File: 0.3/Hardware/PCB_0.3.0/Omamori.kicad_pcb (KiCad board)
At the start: 2 copper layers, 25 x 35 mm, 28 parts, among them J1 Conn_01x04_Female, U1 BQ25570, U3 ATtiny85, U4 TS-1233

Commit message: Unfinished update. Serial communication still unfinished.
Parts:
- removed the U3 at (18.0, 19.5)
- added REF**: Pin_D1.0mm_L10.0mm, Connector_Pin:Pin_D1.0mm_L10.0mm, F.Cu at (25.0, 15.0)
- added U2: ATtiny85-20S, Package_SO:SOIC-8W_5.3x5.3mm_P1.27mm, B.Cu at (18.0, 21.0)
- C_ref1: value 0.01uF -> 10nF
- C_super1: value 640mF -> 1F; footprint own_footprints:Supercap -> own_footprints:Supercap_1F
- moved U3 13.3 mm to (18.0, 15.0), turned to 0 degrees
- moved R_set1 2.38 mm to (32.1, 28.9), turned to 0 degrees
- moved R_set2 2.19 mm to (33.9, 30.4)
- moved R_LED3 1.34 mm to (21.1, 24.7)
- moved R_LED1 0.60 mm to (19.9, 27.7)
- moved R_LED2 0.60 mm to (19.9, 26.2)
- moved C_super1 0.50 mm to (25.0, 37.2)
- renumbered D3 to D1, D1 to D2, D2 to D3, U4 to U3
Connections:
- U3 pad 1: (no net) -> /Reset
- U3 pad 2: /Reset -> GND
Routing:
- net GND: track 183.4 -> 209.4 mm, vias 5 -> 4
- net /Vcc_ATTiny: track 56.5 -> 44.5 mm, vias 0 -> 2
- net /VCC_LED1: track 17.3 -> 9.56 mm
- net Net-(R_set1-Pad2): track 13.0 -> 20.0 mm
- net /Tx: track 30.3 -> 33.3 mm
- net /Reset: track 11.5 -> 14.3 mm
- net /Rx: track 31.9 -> 29.2 mm, vias 2 -> 0
- net Net-(Sol_1-Pad2): track 32.3 -> 34.9 mm
- net /VCC_LED3: track 6.72 -> 9.11 mm
- net /Vr_div: track 4.81 -> 7.13 mm
- net /Vbat: track 29.5 -> 28.7 mm
- net /VCC_LED2: track 10.3 -> 11.0 mm
- net Net-(R_LED1-Pad1): track 7.70 -> 8.30 mm
- net (no net): vias 1 -> 0
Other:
- net class Default removed

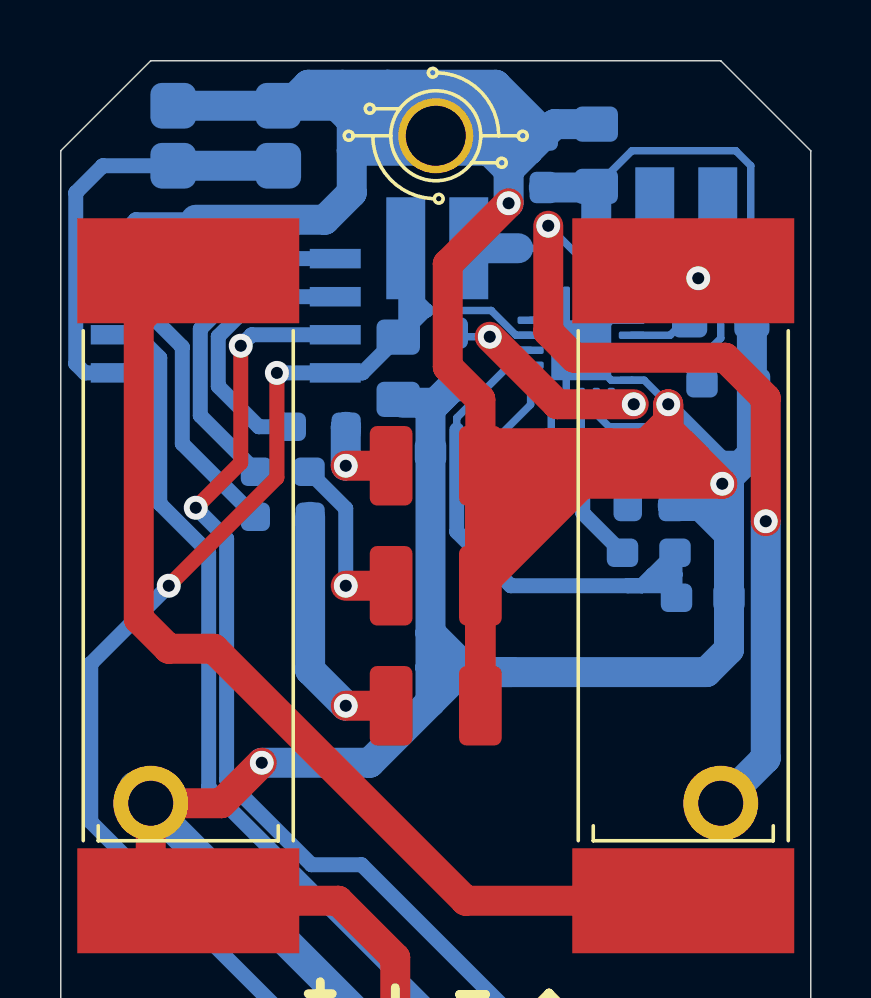
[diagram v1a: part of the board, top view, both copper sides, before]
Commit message: Voltage measurement update.
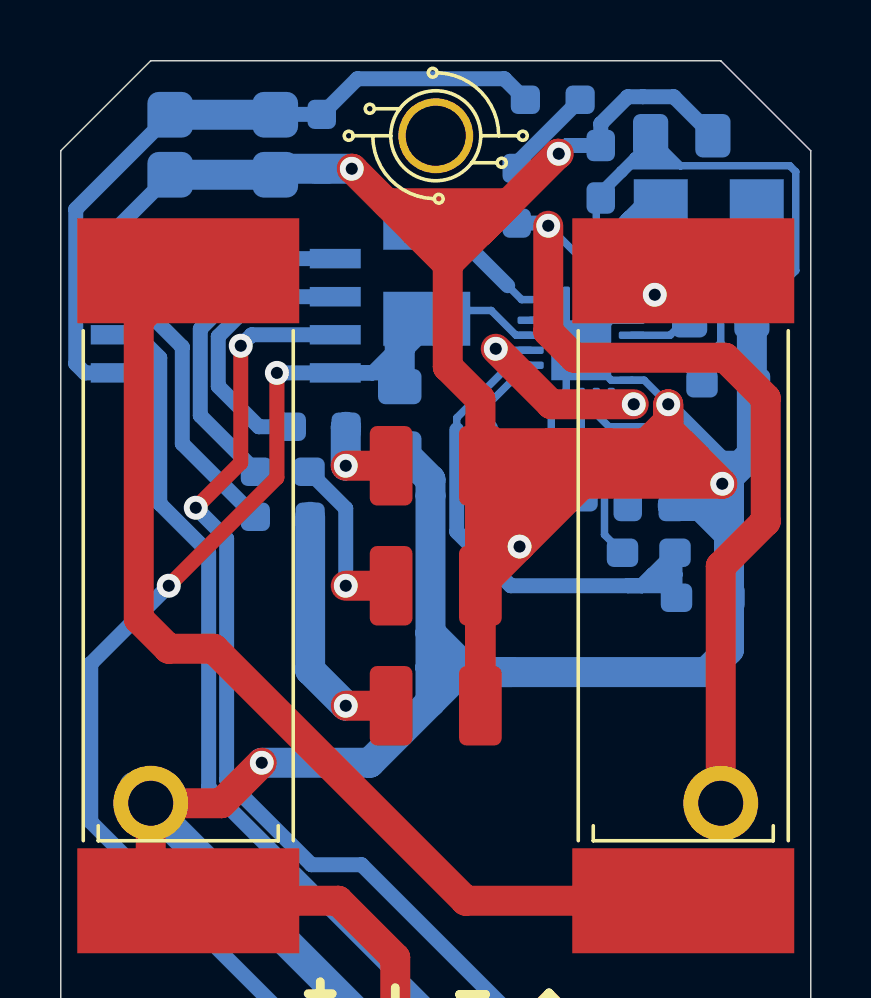
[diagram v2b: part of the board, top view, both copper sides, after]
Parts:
- removed R_pulldown1: 10M, Resistor_SMD:R_0603_1608Metric_Pad1.05x0.95mm_HandSolder
- added R_VDIV1_1: 8.5M, Resistor_SMD:R_0603_1608Metric_Pad0.98x0.95mm_HandSolder, B.Cu at (28.9, 13.8)
- added R_VDIV1_2: 10M, Resistor_SMD:R_0603_1608Metric_Pad0.98x0.95mm_HandSolder, B.Cu at (27.7, 17.0)
- added R_VDIV2: 9M, Resistor_SMD:R_0603_1608Metric_Pad0.98x0.95mm_HandSolder, B.Cu at (21.2, 15.2)
- L_bst1, L_bst2: footprint Inductor_SMD:L_Wuerth_MAPI-3015 -> Inductor_SMD:L_Taiyo-Yuden_NR-30xx_HandSoldering
- moved C_Stor1 2.92 mm to (33.2, 15.0), turned to 0 degrees
- moved C_filter1 1.93 mm to (30.5, 16.2)
- moved C_Stor2 1.65 mm to (23.8, 24.4)
- moved R_ok2 1.52 mm to (29.0, 27.1)
- moved R_ok1 0.97 mm to (26.6, 25.9), turned to -90 degrees
- moved L_bst2 0.83 mm to (24.7, 19.5), turned to -90 degrees
- moved L_bst1 0.76 mm to (34.1, 17.9)
- moved U3 0.32 mm to (17.9, 15.3), turned to 180 degrees
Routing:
- net GND: track 209.4 -> 190.7 mm, vias 4 -> 6
- net /Reset: track 14.3 -> 23.7 mm
- net Net-(L_bst1-Pad2): track 3.86 -> 9.53 mm
- net /Vstor: track 21.0 -> 25.4 mm
- net /Vsolar: track 5.87 -> 9.83 mm
- net Net-(R_VDIV1_1-Pad2): track 0.00 -> 3.28 mm
- net /Vr_div: track 7.13 -> 10.2 mm
- net /Vbat_ok: track 9.33 -> 7.35 mm
- net /Vcc_ATTiny: track 44.5 -> 45.6 mm
- net /Vbat: track 28.7 -> 29.8 mm, vias 2 -> 1
- net Net-(L_bst2-Pad1): track 4.23 -> 5.21 mm
- net Net-(R_ok1-Pad1): track 4.57 -> 5.54 mm
- net Net-(R_ok2-Pad1): track 3.61 -> 4.38 mm

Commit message: Updated hw.
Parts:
- added C_Reset1: 0.1uF, Capacitor_SMD:C_0603_1608Metric_Pad1.08x0.95mm_HandSolder, B.Cu at (69.9, 35.6)
- added C_uC_Filter2: 10nF, Capacitor_SMD:C_0603_1608Metric_Pad1.08x0.95mm_HandSolder, B.Cu at (65.7, 33.0)
- added C_uC_Filter3: 100nF, Capacitor_SMD:C_0603_1608Metric_Pad1.08x0.95mm_HandSolder, B.Cu at (61.4, 32.4)
- added J2: Conn_01x05_Female, Connector_PinHeader_2.54mm:PinHeader_1x05_P2.54mm_Vertical, B.Cu at (70.0, 27.5)
- added J3: Conn_01x06_Female, Connector_PinHeader_2.54mm:PinHeader_1x06_P2.54mm_Vertical, B.Cu at (83.8, 24.1)
- added J4: Conn_01x03_Female, Connector_PinHeader_2.54mm:PinHeader_1x03_P2.54mm_Vertical, B.Cu at (65.8, 27.5)
- added R_Reset1: 10M, Resistor_SMD:R_0603_1608Metric_Pad0.98x0.95mm_HandSolder, B.Cu at (65.5, 35.5)
- C_ref1: footprint Capacitor_SMD:C_0603_1608Metric_Pad1.05x0.95mm_HandSolder -> Capacitor_SMD:C_0603_1608Metric_Pad1.08x0.95mm_HandSolder
- U2: value ATtiny85-20S -> ATtiny1626; footprint Package_SO:SOIC-8W_5.3x5.3mm_P1.27mm -> Package_DFN_QFN:VQFN-20-1EP_3x3mm_P0.4mm_EP1.7x1.7mm
- moved U2 0.71 mm to (17.8, 20.3), turned to 180 degrees
- renumbered C_Stor2 to C_uC_Filter1, D3 to D1, D1 to D3, R_LED3 to R_LED1, R_LED1 to R_LED3
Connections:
- R_LED1 pad 2: /VCC_LED3 -> /VCC_LED1
- R_LED3 pad 2: /VCC_LED1 -> /VCC_LED3
- R_VDIV1_1 pad 1: /Reset -> Net-(R_VDIV1_1-Pad1)
- R_VDIV2 pad 1: /Reset -> Net-(R_VDIV1_1-Pad1)
- U2 pad 1: /Reset -> /VCC_LED1
- U2 pad 2: /Rx -> /VCC_LED2
- U2 pad 3: /VCC_LED1 -> GND
- U2 pad 4: GND -> /Vcc_ATTiny
- U2 pad 5: /VCC_LED2 -> /VCC_LED3
- U2 pad 6: /VCC_LED3 -> Net-(J3-Pad1)
- U2 pad 7: /Tx -> Net-(J3-Pad2)
- U2 pad 8: /Vcc_ATTiny -> Net-(J3-Pad3)
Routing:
- net /Reset: track 23.7 -> 12.6 mm
- net /VCC_LED2: track 11.0 -> 0.00 mm
- net /VCC_LED1: track 9.56 -> 0.00 mm
- net /VCC_LED3: track 9.11 -> 0.00 mm
- net /Tx: track 33.3 -> 26.1 mm, vias 2 -> 1
- net Net-(D3-Pad2): track 8.30 -> 1.51 mm
- net /Rx: track 29.2 -> 22.6 mm
- net Net-(D2-Pad2): track 5.82 -> 1.51 mm
- net GND: track 190.7 -> 187.2 mm
- net Net-(D1-Pad2): track 2.82 -> 1.53 mm

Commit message: Moved some parts.
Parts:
- moved J4 50.6 mm to (15.2, 25.4)
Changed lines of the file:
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@@
   )
   (footprint "Connector_PinHeader_2.54mm:PinHeader_1x03_P2.54mm_Vertical" (layer "B.Cu")
-    (at 65.827618 27.53 180)
+    (at 15.24 25.4 180)
     (descr "Through hole straight pin header, 1x03, 2.54mm pitch, single row")
     (tags "Through hole pin header THT 1x03 2.54mm single row")

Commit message: Temporarily finished pcb design.
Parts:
- removed the J1 at (28.8, 45.5)
- removed J3: Conn_01x06_Female, Connector_PinHeader_2.54mm:PinHeader_1x06_P2.54mm_Vertical
- removed R_LED1, R_LED3: 500, Resistor_SMD:R_0603_1608Metric_Pad0.98x0.95mm_HandSolder
- removed R_LED2: 500, Resistor_SMD:R_0603_1608Metric_Pad1.05x0.95mm_HandSolder
- J2: value Conn_01x05_Female -> Conn_01x07_Female; footprint Connector_PinHeader_2.54mm:PinHeader_1x05_P2.54mm_Vertical -> Connector_PinHeader_2.54mm:PinHeader_1x07_P2.54mm_Vertical; moved to F.Cu
- moved C_Reset1 57.3 mm to (14.3, 21.5), turned to -90 degrees
- moved J2 55.4 mm to (17.4, 45.0), turned to 90 degrees
- moved R_Reset1 54.1 mm to (14.3, 18.2), turned to -90 degrees
- moved C_uC_Filter2 45.1 mm to (22.0, 22.0), turned to -90 degrees
- moved C_uC_Filter3 41.7 mm to (22.0, 18.6), turned to 90 degrees
- moved J1 5.03 mm to (15.2, 30.4), turned to 0 degrees
- moved R_VDIV2 3.36 mm to (19.5, 18.1), turned to 0 degrees
- moved U2 1.08 mm to (17.8, 21.4)
- renumbered J4 to J1
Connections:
- D1 pad 2: Net-(D1-Pad2) -> /VCC_LED1
- D2 pad 2: Net-(D2-Pad2) -> /VCC_LED2
- D3 pad 2: Net-(D3-Pad2) -> /VCC_LED3
- J1 pad 1: /Vcc_ATTiny -> GND
- J1 pad 3: GND -> /Vcc_ATTiny
- J2 pad 1: Net-(J2-Pad1) -> GND
- J2 pad 2: Net-(J2-Pad2) -> /Vcc_ATTiny
- J2 pad 3: Net-(J2-Pad3) -> /Rx
- J2 pad 4: Net-(J2-Pad4) -> /Tx
- J2 pad 5: Net-(J2-Pad5) -> Net-(U2-Pad8)
- U2 pad 10: Net-(J2-Pad3) -> unconnected-(U2-Pad10)
- U2 pad 11: Net-(J2-Pad2) -> unconnected-(U2-Pad11)
- U2 pad 12: Net-(J2-Pad1) -> unconnected-(U2-Pad12)
- U2 pad 13: /Rx -> /Tx
- U2 pad 14: /Tx -> /Rx
- U2 pad 16: Net-(J3-Pad5) -> unconnected-(U2-Pad16)
- U2 pad 17: Net-(J3-Pad4) -> unconnected-(U2-Pad17)
- U2 pad 18: Net-(J2-Pad5) -> unconnected-(U2-Pad18)
- U2 pad 6: Net-(J3-Pad1) -> Net-(J2-Pad7)
- U2 pad 7: Net-(J3-Pad2) -> Net-(J2-Pad6)
- U2 pad 8: Net-(J3-Pad3) -> Net-(U2-Pad8)
- U2 pad 9: Net-(J2-Pad4) -> unconnected-(U2-Pad9)
- U3 pad 1: /Reset -> GND
- U3 pad 2: GND -> /Reset
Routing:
- net GND: track 187.2 -> 217.1 mm, vias 6 -> 8
- net Net-(J2-Pad7): track 0.00 -> 28.7 mm
- net Net-(J2-Pad6): track 0.00 -> 27.1 mm
- net Net-(U2-Pad8): track 0.00 -> 26.2 mm
- net Net-(R_VDIV1_1-Pad1): track 0.00 -> 17.1 mm
- net Net-(C_Reset1-Pad1): track 0.00 -> 16.2 mm
- net /VCC_LED3: track 0.00 -> 14.5 mm, vias 0 -> 1
- net Net-(Sol_1-Pad2): track 34.9 -> 47.1 mm, vias 0 -> 2
- net /VCC_LED2: track 0.00 -> 12.1 mm, vias 0 -> 1
- net /Reset: track 12.6 -> 2.26 mm
- net /VCC_LED1: track 0.00 -> 8.86 mm, vias 0 -> 1
- net /Rx: track 22.6 -> 28.0 mm
- net /Tx: track 26.1 -> 28.2 mm, vias 1 -> 0
- net /Vcc_ATTiny: track 45.6 -> 47.4 mm, vias 2 -> 3
- net Net-(D1-Pad2): track 1.53 -> 0.00 mm, vias 1 -> 0
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
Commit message: Updated pcb.
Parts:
- D1, D2, D3: footprint LED_SMD:LED_1210_3225Metric_Pad1.42x2.65mm_HandSolder -> LED_SMD:LED_0805_2012Metric
- moved C_Reset1 3.89 mm to (16.2, 18.1), turned to 180 degrees
- moved R_Reset1 3.22 mm to (15.7, 15.3)
- moved U3 1.10 mm to (19.0, 15.2)
- moved D1 0.80 mm to (25.0, 25.2)
- moved D3 0.80 mm to (25.0, 34.8)
- moved U2 0.13 mm to (17.6, 21.4)
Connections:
- U2 pad 10: unconnected-(U2-Pad10) -> /Rx
- U2 pad 13: /Tx -> unconnected-(U2-Pad13)
- U2 pad 14: /Rx -> unconnected-(U2-Pad14)
- U2 pad 9: unconnected-(U2-Pad9) -> /Tx
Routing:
- net GND: track 217.1 -> 269.8 mm, vias 8 -> 9
- net /Rx: track 28.0 -> 24.5 mm
- net /Tx: track 28.2 -> 25.4 mm
- net /VCC_LED3: track 14.5 -> 16.3 mm
- net /VCC_LED2: track 12.1 -> 13.3 mm
- net Net-(R_VDIV1_1-Pad1): track 17.1 -> 16.1 mm
- net Net-(J2-Pad7): track 28.7 -> 29.2 mm
